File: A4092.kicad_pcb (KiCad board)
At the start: 2 copper layers, 192.7 x 123.3 mm, 103 parts, among them CN1 Zorro3, J1 Conn_02x25_Odd_Even, J2 Conn_01x06_Pin, J3 TO-LED, J4 TO-MB, J5 5787170-5, J6 350543-1, J7 22112042, SW1 219-8MST, U1 CY74FCT16543TPVCT, U10 SN74F244DB, U11 SN74ABT16374ADGGR, U12 74LVC07APW_118, U13 SN74ABT16245ADGGR, U14 74ACT521MTCX, U15 74ABT74, U2 CY74FCT16543TPVCT, U3 CY74FCT16543TPVCT, U4 NCR53c710 SCSI Host Controller, U5 CY74FCT543ATQCT, U6 ATF1508AS-10AU100, U7 SST39SF010, U8 DS21S07A, U9 DS21S07A, Y1 Abracon ACO-50MHz

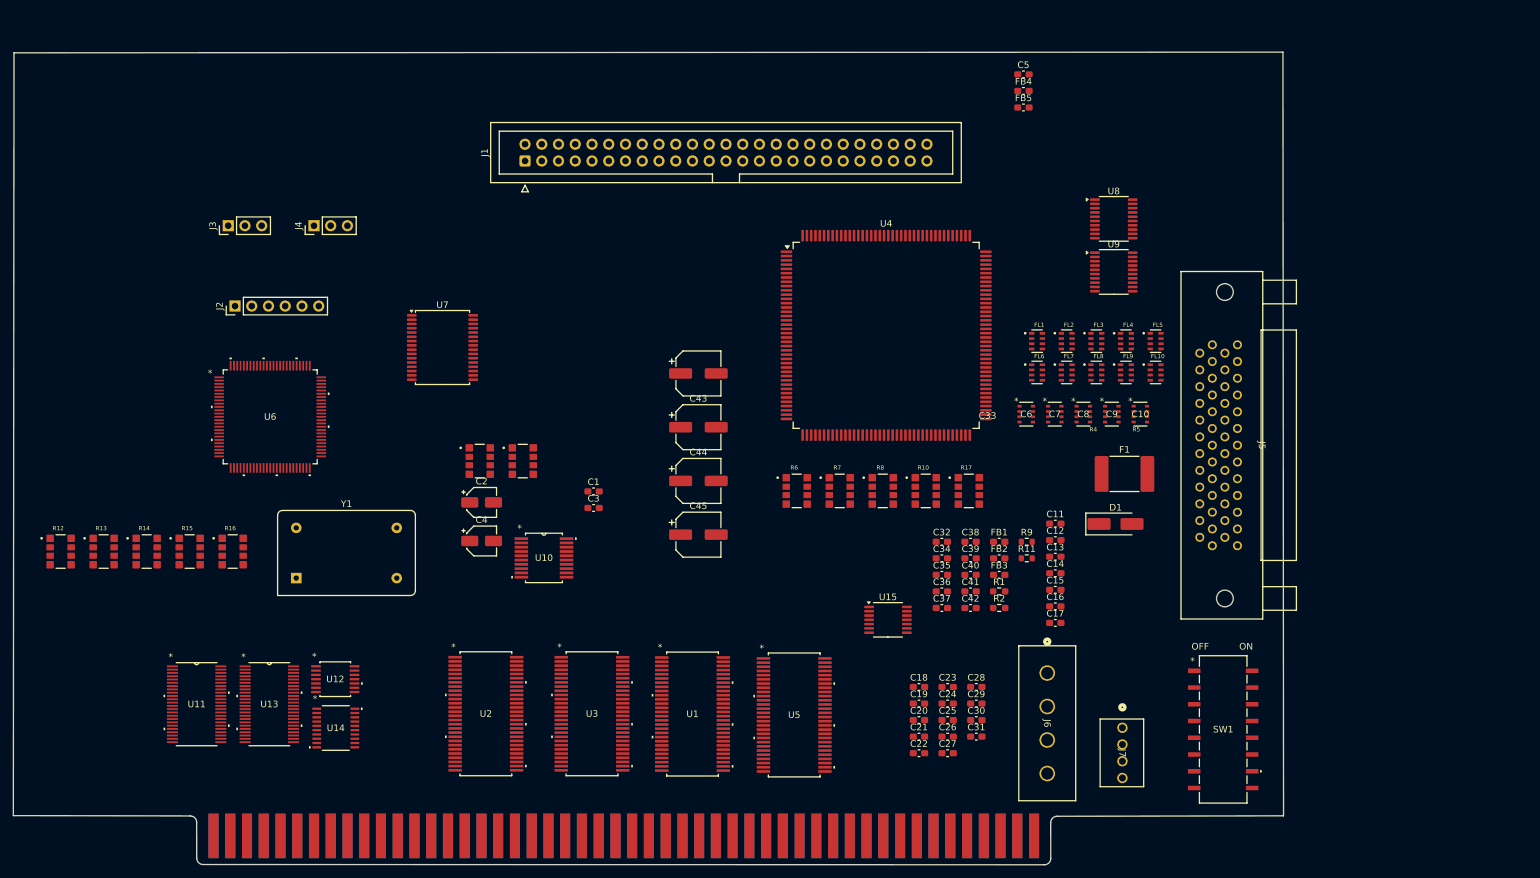
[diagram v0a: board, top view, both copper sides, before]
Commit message: Update RN footprint to CAY16_102J4LF
- Rename RNs from R to RN.
- Fix U5 footprint
- Rename pages to be consecutive numbers
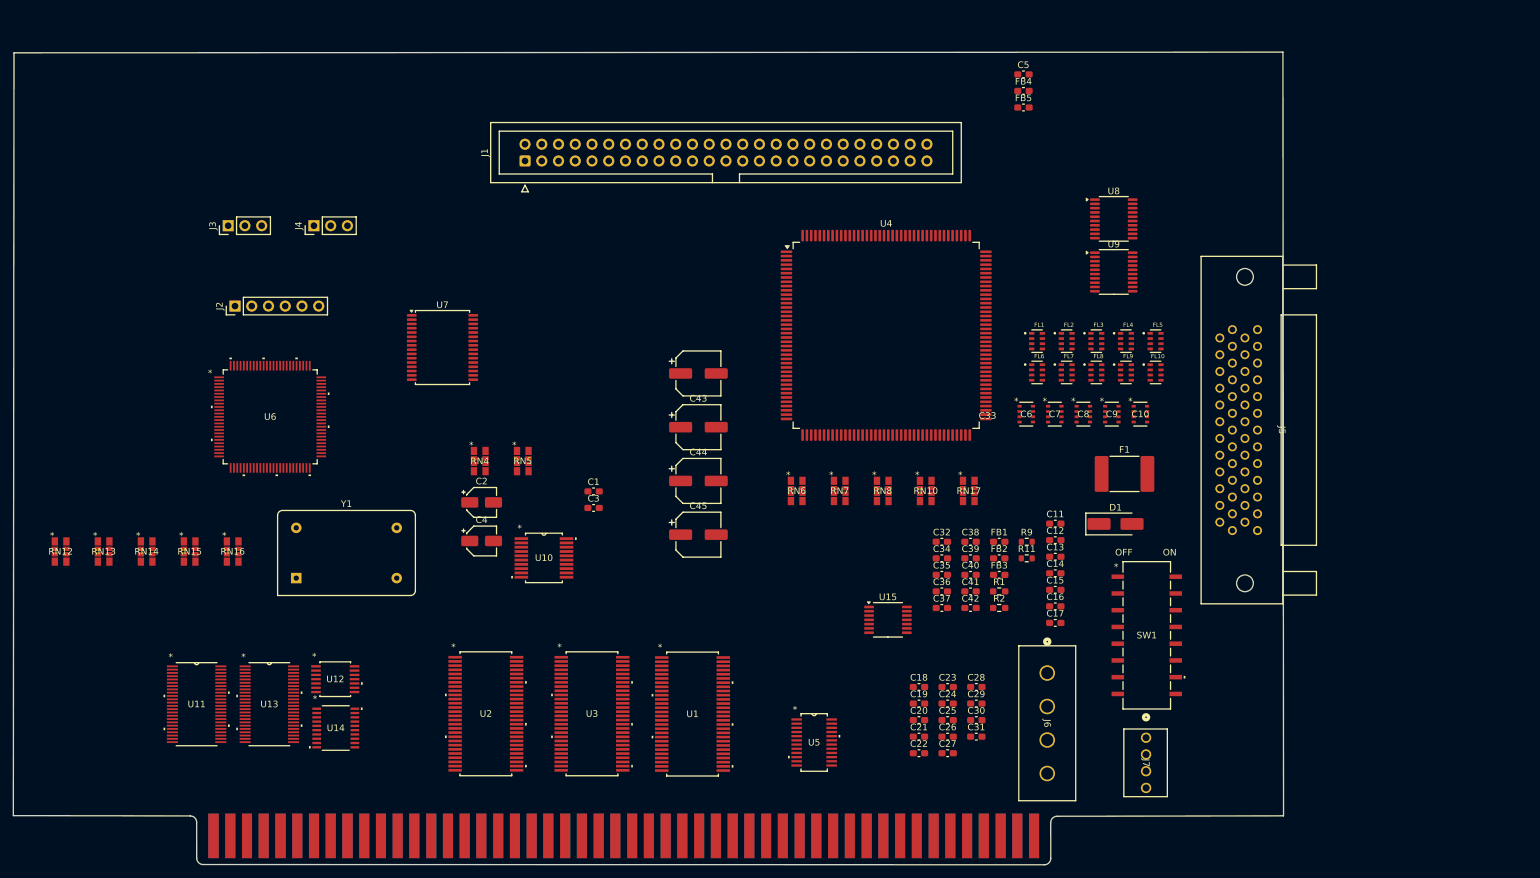
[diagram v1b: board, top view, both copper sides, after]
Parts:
- RN10: renamed from R10; footprint YC324-FK-071KL:RESCAXS127P508X320X70-8N -> CAY16_102J4LF:BO_CAY16
- RN12: renamed from R12; footprint YC324-FK-071KL:RESCAXS127P508X320X70-8N -> CAY16_102J4LF:BO_CAY16
- RN13: renamed from R13; footprint YC324-FK-071KL:RESCAXS127P508X320X70-8N -> CAY16_102J4LF:BO_CAY16
- RN14: renamed from R14; footprint YC324-FK-071KL:RESCAXS127P508X320X70-8N -> CAY16_102J4LF:BO_CAY16
- RN15: renamed from R15; footprint YC324-FK-071KL:RESCAXS127P508X320X70-8N -> CAY16_102J4LF:BO_CAY16
- RN16: renamed from R16; footprint YC324-FK-071KL:RESCAXS127P508X320X70-8N -> CAY16_102J4LF:BO_CAY16
- RN17: renamed from R17; footprint YC324-FK-071KL:RESCAXS127P508X320X70-8N -> CAY16_102J4LF:BO_CAY16
- RN4: renamed from R4; value YC324-FK-071KL -> 1K; footprint YC324-FK-071KL:RESCAXS127P508X320X70-8N -> CAY16_102J4LF:BO_CAY16
- RN5: renamed from R5; value YC324-FK-071KL -> 1K; footprint YC324-FK-071KL:RESCAXS127P508X320X70-8N -> CAY16_102J4LF:BO_CAY16
- RN6: renamed from R6; footprint YC324-FK-071KL:RESCAXS127P508X320X70-8N -> CAY16_102J4LF:BO_CAY16
- RN7: renamed from R7; footprint YC324-FK-071KL:RESCAXS127P508X320X70-8N -> CAY16_102J4LF:BO_CAY16
- RN8: renamed from R8; footprint YC324-FK-071KL:RESCAXS127P508X320X70-8N -> CAY16_102J4LF:BO_CAY16
- U5: footprint 74FCT16543:DL56 -> CY74FCT543ATQCT:DBQ24
- moved SW1 18.4 mm to (204.1, 121.9)
- moved U5 5.16 mm to (153.7, 138.1)
- moved J7 3.89 mm to (204.0, 137.4)
- moved J5 3.82 mm to (220.9, 75.5)

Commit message: Connect VCCINT on CPLD, add GND and V5 to power symbols
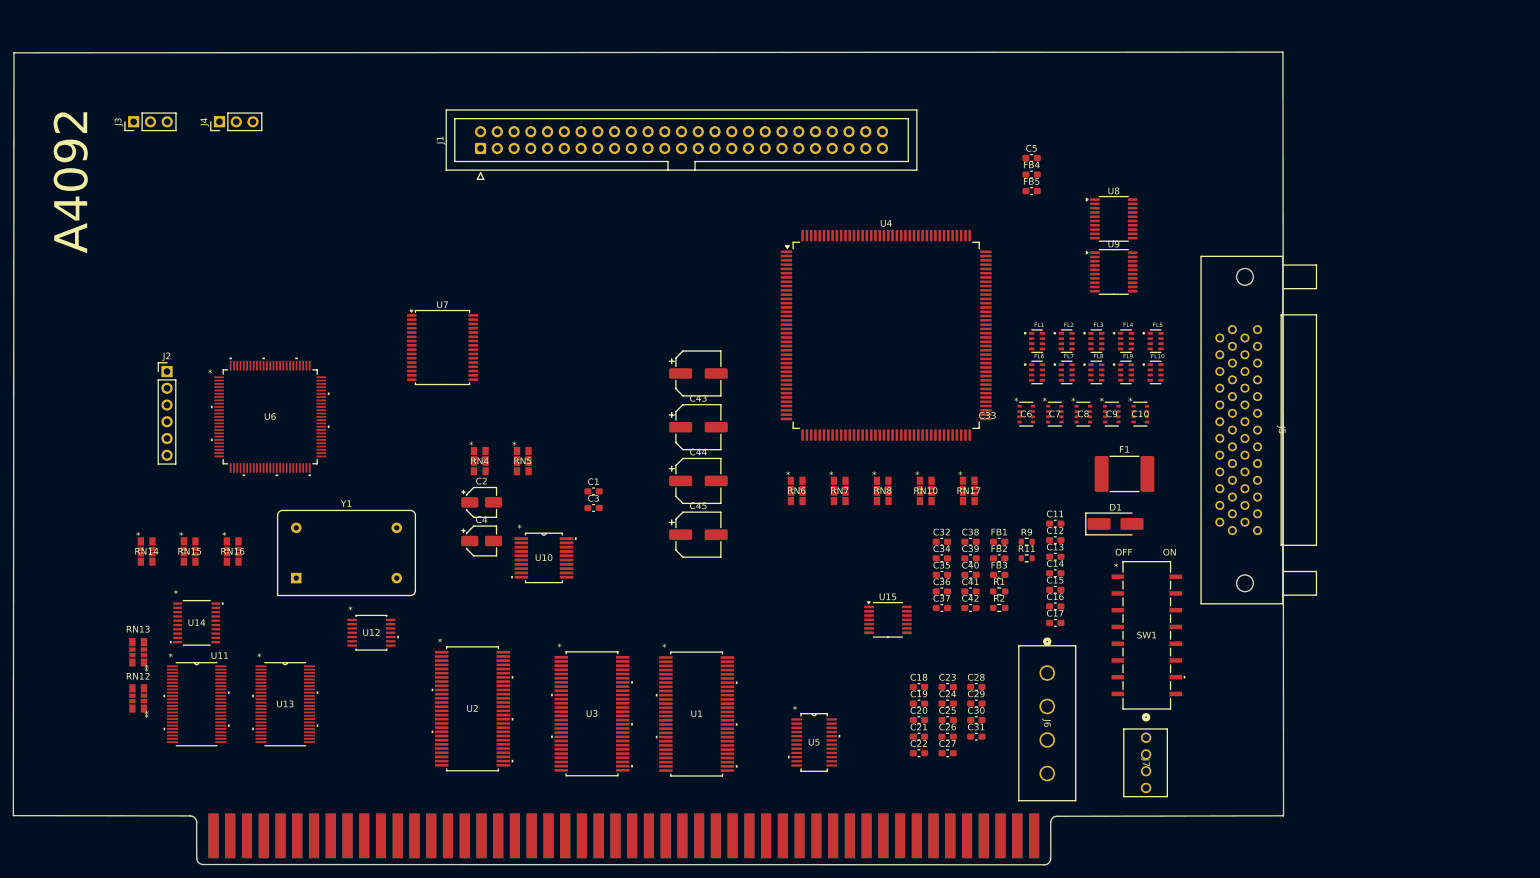
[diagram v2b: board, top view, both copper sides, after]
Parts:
- moved U14 26.4 mm to (60.0, 120.0)
- moved RN12 25.2 mm to (51.1, 131.5), turned to 180 degrees
- moved J3 21.3 mm to (50.5, 44.0)
- moved J4 21.3 mm to (63.5, 44.0)
- moved RN13 16.2 mm to (51.1, 124.5), turned to 180 degrees
- moved J2 14.3 mm to (55.5, 81.9), turned to 0 degrees
- moved C5 12.7 mm to (186.6, 49.5)
- moved FB4 12.7 mm to (186.6, 52.0)
- moved FB5 12.7 mm to (186.6, 54.5)
- moved U12 8.92 mm to (86.5, 121.5)
- moved J1 7.00 mm to (103.1, 48.0)
- moved U13 2.41 mm to (73.4, 132.3)
- moved U2 2.17 mm to (101.8, 133.0)
- moved U1 0.63 mm to (135.8, 133.8)
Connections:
- U6 pad 91: unconnected-(U6-VCCINT-Pad91) -> V5
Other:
- board text added: "A4092"

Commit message: Incorporate Feedback from LIV2
- Move CLK, CLKI, Z_7M to GCLK1, GCLK2, GCLK3
  as they are connected to all macro cells.
- OE1 and GCLR on the 1508 are input only, move FC0/FC1 there.

Also found two duplicate signals on the ATF1508, consolidated them.
This leaves us with 8 free I/Os at the moment.
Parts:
- U1, U2, U3: value CY74FCT16543TPVCT -> SN74ABT16543DGGR
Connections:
- U6 pad 25: unconnected-(U6-I/O-Pad25) -> PLD_NOZ3
- U6 pad 37: unconnected-(U6-I/O-Pad37) -> Z_CINH
- U6 pad 41: PLD_INTVEC -> Z_SENSEZ3
- U6 pad 52: CLK -> PLD_CFGLT
- U6 pad 53: CLKI -> PLD_MTCR
- U6 pad 55: PLD_NOZ3 -> MATCH
- U6 pad 58: PLD_MTCR -> PLD_INTSPC
- U6 pad 72: PLD_INTSPC -> BMASTER
- U6 pad 83: PLD_FC1 -> SBR
- U6 pad 84: PLD_FC0 -> SBG
- U6 pad 85: Z_SENSEZ3 -> Z_7M
- U6 pad 87: PLD_CFGLT -> CLK
- U6 pad 88: Z_CINH -> PLD_FC1
- U6 pad 89: MATCH -> PLD_FC0
- U6 pad 90: PLD_NOZ3 -> CLKI
- U6 pad 94: BMASTER -> unconnected-(U6-I/O-Pad94)
- U6 pad 96: SBR -> unconnected-(U6-I/O-Pad96)
- U6 pad 97: SBG -> unconnected-(U6-I/O-Pad97)
- U6 pad 98: Z_7M -> unconnected-(U6-I/O-Pad98)
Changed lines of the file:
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@@
 	(net 320 "PLD_NACK")
 	(net 321 "Z_FCS_TO_FB")
-	(net 322 "unconnected-(U6-I{slash}O-Pad25)")
+	(net 322 "unconnected-(U6-I{slash}O-Pad98)")
 	(net 323 "MATCH")
 	(net 324 "PLD_SCSI")
@@
 	(net 332 "unconnected-(U6-I{slash}O{slash}PD1-Pad1)")
 	(net 333 "unconnected-(U6-I{slash}O-Pad100)")
-	(net 334 "unconnected-(U6-I{slash}O-Pad37)")
+	(net 334 "unconnected-(U6-I{slash}O-Pad94)")
 	(net 335 "PLD_INTREG")
 	(net 336 "ROM_OE")
@@
 	(net 354 "unconnected-(RN16-Pad3)")
 	(net 355 "unconnected-(RN16-Pad6)")
+	(net 356 "unconnected-(U6-I{slash}O-Pad97)")
+	(net 357 "unconnected-(U6-I{slash}O-Pad96)")
 	(footprint "Capacitor_SMD:C_0603_1608Metric_Pad1.08x0.95mm_HandSolder"
 		(layer "F.Cu")
@@
 			)
 		)
-		(property "Value" "CY74FCT16543TPVCT"
+		(property "Value" "SN74ABT16543DGGR"
 			(at 0 0 0)
 			(unlocked yes)
@@
 			)
 		)
-		(property "Datasheet" "CY74FCT16543TPVCT"
+		(property "Datasheet" "https://www.ti.com/lit/ds/symlink/sn74abt16543.pdf"
 			(at 0 0 0)
 			(layer "F.Fab")
@@
 			(size 0.27 1.4612)
 			(layers "F.Cu" "F.Mask" "F.Paste")
-			(net 322 "unconnected-(U6-I{slash}O-Pad25)")
+			(net 326 "PLD_NOZ3")
 			(pinfunction "I/O")
 			(pintype "bidirectional")
@@
 			(size 0.27 1.4612)
 			(layers "F.Cu" "F.Mask" "F.Paste")
-			(net 334 "unconnected-(U6-I{slash}O-Pad37)")
+			(net 52 "Z_CINH")
 			(pinfunction "I/O")
 			(pintype "bidirectional")
@@
 			(size 0.27 1.4612)
 			(layers "F.Cu" "F.Mask" "F.Paste")
-			(net 315 "PLD_INTVEC")
+			(net 331 "Z_SENSEZ3")
 			(pinfunction "I/O/PD2")
 			(pintype "bidirectional")
@@
 			(size 0.27 1.4612)
 			(layers "F.Cu" "F.Mask" "F.Paste")
-			(net 176 "CLK")
+			(net 337 "PLD_CFGLT")
 			(pinfunction "I/O")
 			(pintype "bidirectional")
@@
 			(size 0.27 1.4612)
 			(layers "F.Cu" "F.Mask" "F.Paste")
-			(net 175 "CLKI")
+			(net 219 "PLD_MTCR")
 			(pinfunction "I/O")
 			(pintype "bidirectional")
@@
 			(size 0.27 1.4612)
 			(layers "F.Cu" "F.Mask" "F.Paste")
-			(net 326 "PLD_NOZ3")
+			(net 323 "MATCH")
 			(pinfunction "I/O")
 			(pintype "bidirectional")
@@
 			(size 0.27 1.4612)
 			(layers "F.Cu" "F.Mask" "F.Paste")
-			(net 219 "PLD_MTCR")
+			(net 313 "PLD_INTSPC")
 			(pinfunction "I/O")
 			(pintype "bidirectional")
@@
 			(size 0.27 1.4612)
 			(layers "F.Cu" "F.Mask" "F.Paste")
-			(net 313 "PLD_INTSPC")
+			(net 270 "BMASTER")
 			(pinfunction "I/O")
 			(pintype "bidirectional")
@@
 			(size 0.27 1.4612)
 			(layers "F.Cu" "F.Mask" "F.Paste")
-			(net 213 "PLD_FC1")
+			(net 111 "SBR")
 			(pinfunction "I/O")
 			(pintype "bidirectional")
@@
 			(size 0.27 1.4612)
 			(layers "F.Cu" "F.Mask" "F.Paste")
-			(net 211 "PLD_FC0")
+			(net 289 "SBG")
 			(pinfunction "I/O")
 			(pintype "bidirectional")
@@
 			(size 0.27 1.4612)
 			(layers "F.Cu" "F.Mask" "F.Paste")
-			(net 331 "Z_SENSEZ3")
+			(net 80 "Z_7M")
 			(pinfunction "I/O/GCLK3")
 			(pintype "bidirectional")
@@
 			(size 0.27 1.4612)
 			(layers "F.Cu" "F.Mask" "F.Paste")
-			(net 337 "PLD_CFGLT")
+			(net 176 "CLK")
 			(pinfunction "INPUT/GCLK1")
 			(pintype "bidirectional")
@@
 			(size 0.27 1.4612)
 			(layers "F.Cu" "F.Mask" "F.Paste")
-			(net 52 "Z_CINH")
+			(net 213 "PLD_FC1")
 			(pinfunction "INPUT/OE1")
 			(pintype "bidirectional")
@@
 			(size 0.27 1.4612)
 			(layers "F.Cu" "F.Mask" "F.Paste")
-			(net 323 "MATCH")
+			(net 211 "PLD_FC0")
 			(pinfunction "INPUT/GCLR")
 			(pintype "bidirectional")
@@
 			(size 0.27 1.4612)
 			(layers "F.Cu" "F.Mask" "F.Paste")
-			(net 326 "PLD_NOZ3")
+			(net 175 "CLKI")
 			(pinfunction "INPUT/OE2/GCLK2")
 			(pintype "bidirectional")
@@
 			(size 0.27 1.4612)
 			(layers "F.Cu" "F.Mask" "F.Paste")
-			(net 270 "BMASTER")
+			(net 334 "unconnected-(U6-I{slash}O-Pad94)")
 			(pinfunction "I/O")
 			(pintype "bidirectional")
@@
 			(size 0.27 1.4612)
 			(layers "F.Cu" "F.Mask" "F.Paste")
-			(net 111 "SBR")
+			(net 357 "unconnected-(U6-I{slash}O-Pad96)")
 			(pinfunction "I/O")
 			(pintype "bidirectional")
@@
 			(size 0.27 1.4612)
 			(layers "F.Cu" "F.Mask" "F.Paste")
-			(net 289 "SBG")
+			(net 356 "unconnected-(U6-I{slash}O-Pad97)")
 			(pinfunction "I/O")
 			(pintype "bidirectional")
@@
 			(size 0.27 1.4612)
 			(layers "F.Cu" "F.Mask" "F.Paste")
-			(net 80 "Z_7M")
+			(net 322 "unconnected-(U6-I{slash}O-Pad98)")
 			(pinfunction "I/O")
 			(pintype "bidirectional")
@@
 			)
 		)
-		(property "Value" "CY74FCT16543TPVCT"
+		(property "Value" "SN74ABT16543DGGR"
 			(at 0 0 0)
 			(unlocked yes)
@@
 			)
 		)
-		(property "Datasheet" "CY74FCT16543TPVCT"
+		(property "Datasheet" "https://www.ti.com/lit/ds/symlink/sn74abt16543.pdf"
 			(at 0 0 0)
 			(layer "F.Fab")
@@
 			)
 		)
-		(property "Value" "CY74FCT16543TPVCT"
+		(property "Value" "SN74ABT16543DGGR"
 			(at 0 0 0)
 			(unlocked yes)
@@
 			)
 		)
-		(property "Datasheet" "CY74FCT16543TPVCT"
+		(property "Datasheet" "https://www.ti.com/lit/ds/symlink/sn74abt16543.pdf"
 			(at 0 0 0)
 			(layer "F.Fab")

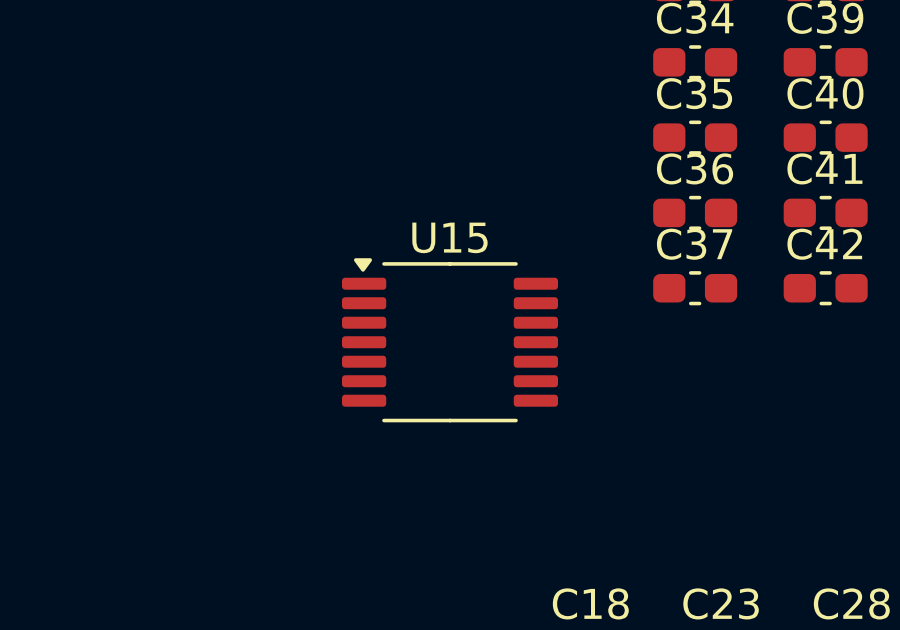
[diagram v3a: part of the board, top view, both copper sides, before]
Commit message: Drop 74ABT74
The 74ABT74 is only used as a divider to create 25MHz from the 50MHz clock, and
it can be removed. Instead, the 50MHz are directly brought to the ATF1508. CLK
will be used as an output, not an input, so move away from GCLK pin. CLKI is no
longer needed on a pin as it doesn't connect to anything anymore.
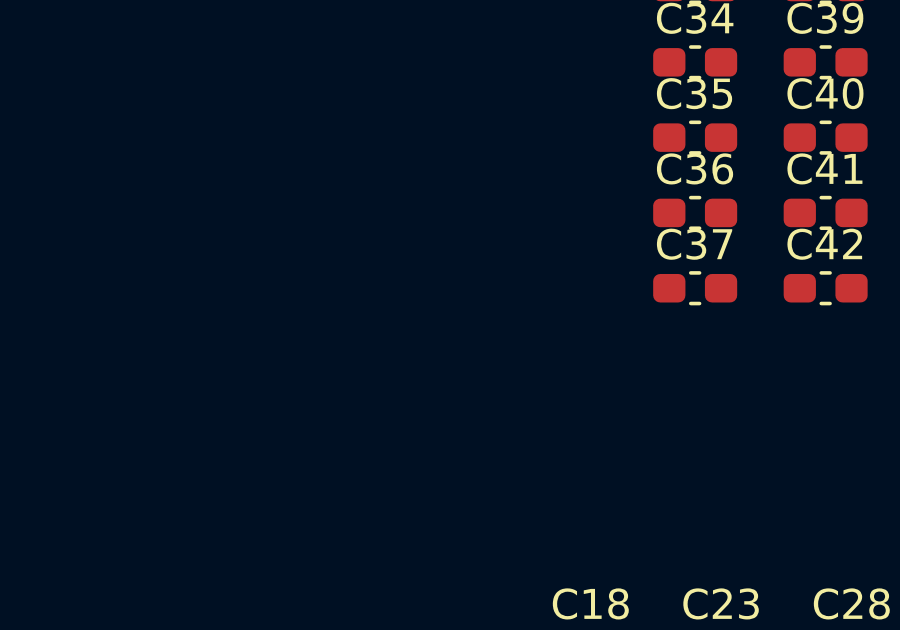
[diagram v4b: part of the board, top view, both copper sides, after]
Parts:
- removed U15: 74ABT74, Package_SO:TSSOP-14_4.4x5mm_P0.65mm
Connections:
- U6 pad 76: Z_MTACK -> CLK
- U6 pad 87: CLK -> CLK_50M
- U6 pad 90: CLKI -> Z_MTACK
